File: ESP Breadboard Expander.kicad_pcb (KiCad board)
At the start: 2 copper layers, 88.3 x 51 mm, 20 parts, among them J1 Conn_02x04_Odd_Even, J10 PJ-063BH, J2 Conn_01x08_Socket, J3 Conn_01x08_Socket, J4 Conn_01x19_Socket, J5 Conn_01x19_Socket, J6 Conn_01x14_Pin, J7 Conn_01x14_Pin, J8 Conn_01x02_Pin, J9 Conn_01x02_Pin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

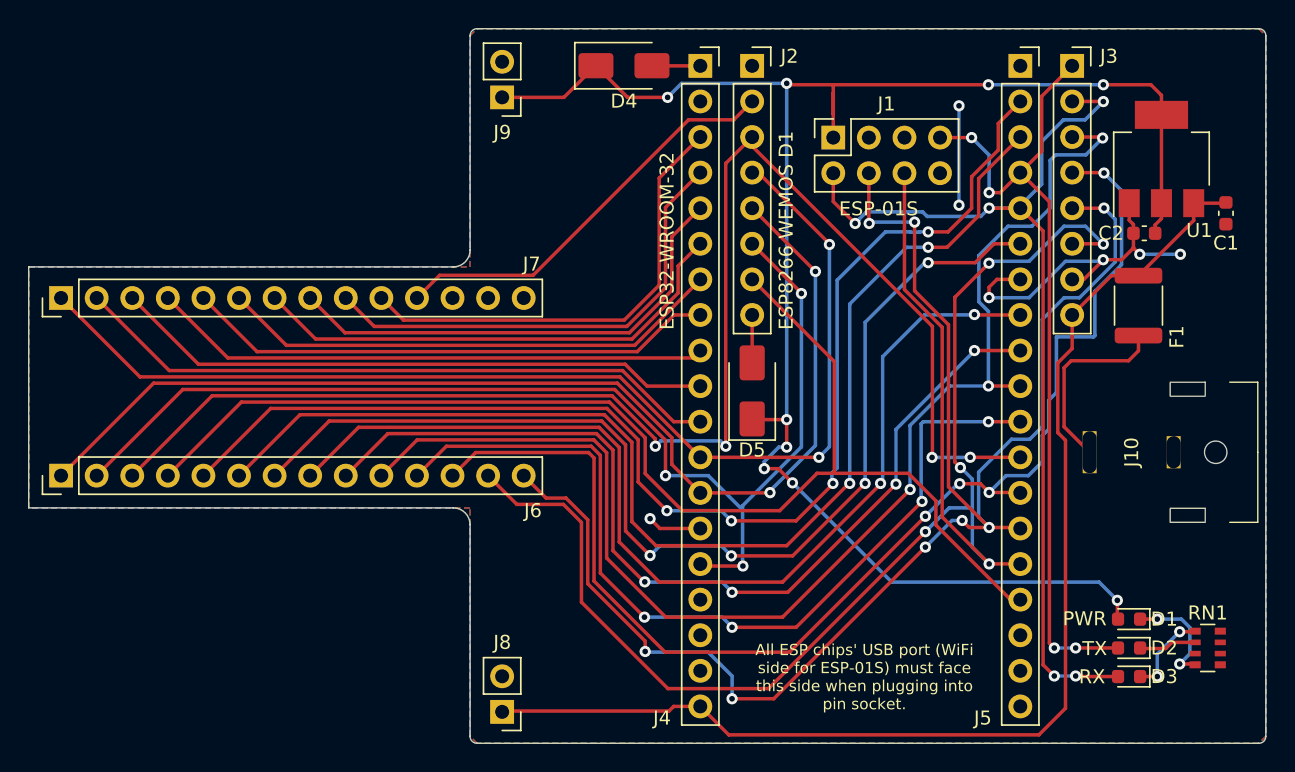
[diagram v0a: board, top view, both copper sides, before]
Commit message: Removed diode for 3.3V power from ESP to breadboard
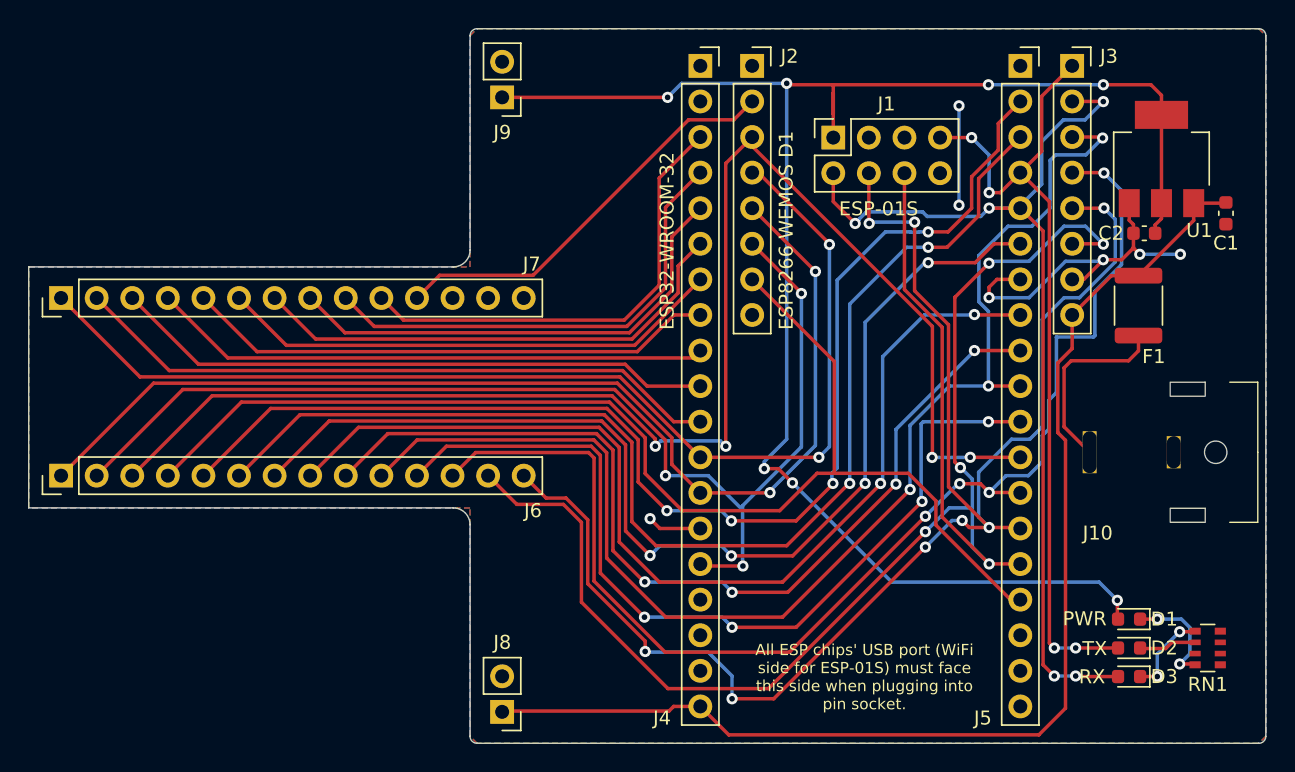
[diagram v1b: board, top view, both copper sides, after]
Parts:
- removed D4, D5: D_Small, Diode_SMD:D_SMA
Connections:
- J2 pad 8: Net-(D5-A) -> unconnected-(J2-Pin_8-Pad8)
- J4 pad 1: Net-(D4-A) -> unconnected-(J4-Pin_1-Pad1)
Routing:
- net +3.3V: track 126.5 -> 121.8 mm, vias 9 -> 7
- net Net-(D4-A): track 3.45 -> 0.00 mm
- net Net-(D5-A): track 3.42 -> 0.00 mm

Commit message: Improved GND traces
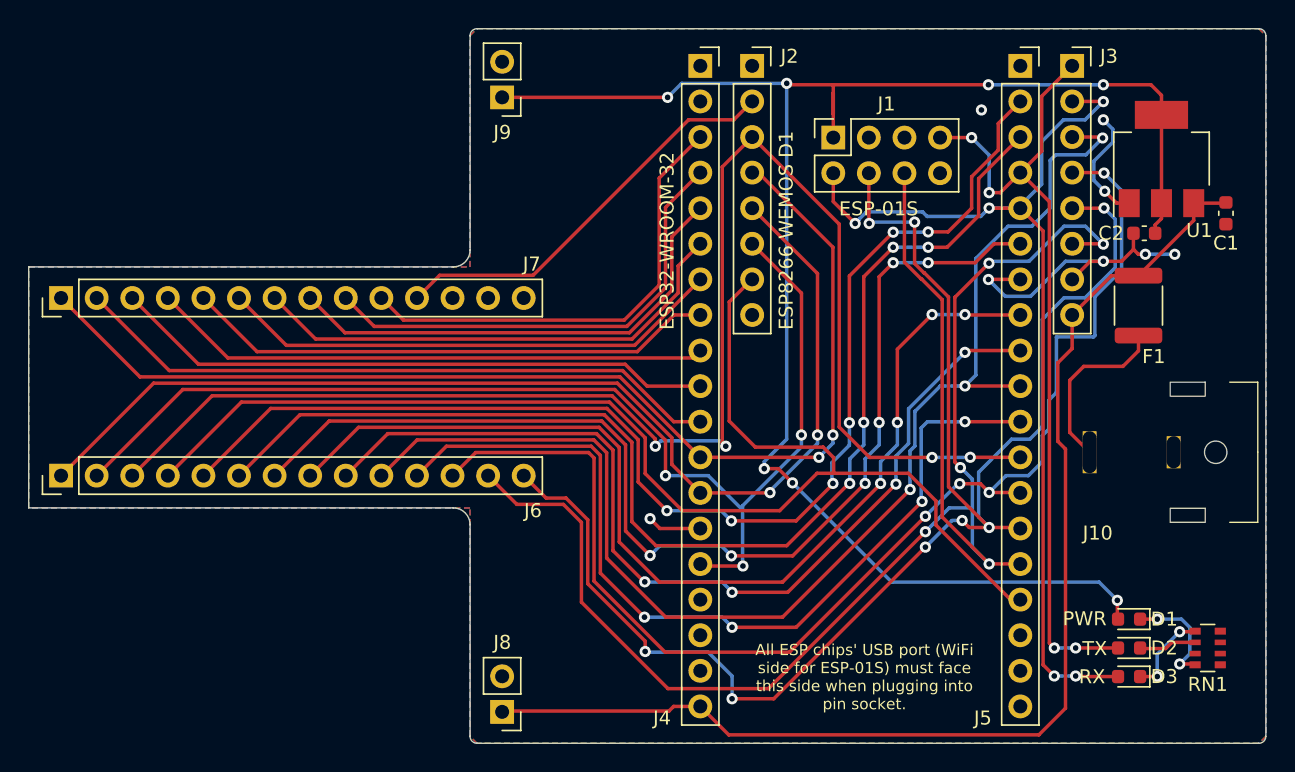
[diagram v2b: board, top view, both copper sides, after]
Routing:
- net /IO15: track 89.9 -> 94.0 mm
- net /IO16: track 104.2 -> 107.0 mm
- net GND: track 35.6 -> 33.8 mm, vias 7 -> 8
- net /IO21: track 79.0 -> 80.3 mm, vias 4 -> 6
- net Net-(F1-Pad1): track 13.8 -> 12.7 mm
- net /IO22: track 85.9 -> 86.4 mm, vias 2 -> 4
- net /IO5: track 91.9 -> 92.5 mm
- net /IO23: track 88.6 -> 88.3 mm, vias 4 -> 6
- net /IO19: track 73.8 -> 73.5 mm, vias 2 -> 4

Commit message: Added more labeling & checked some JLCPCB capabilities
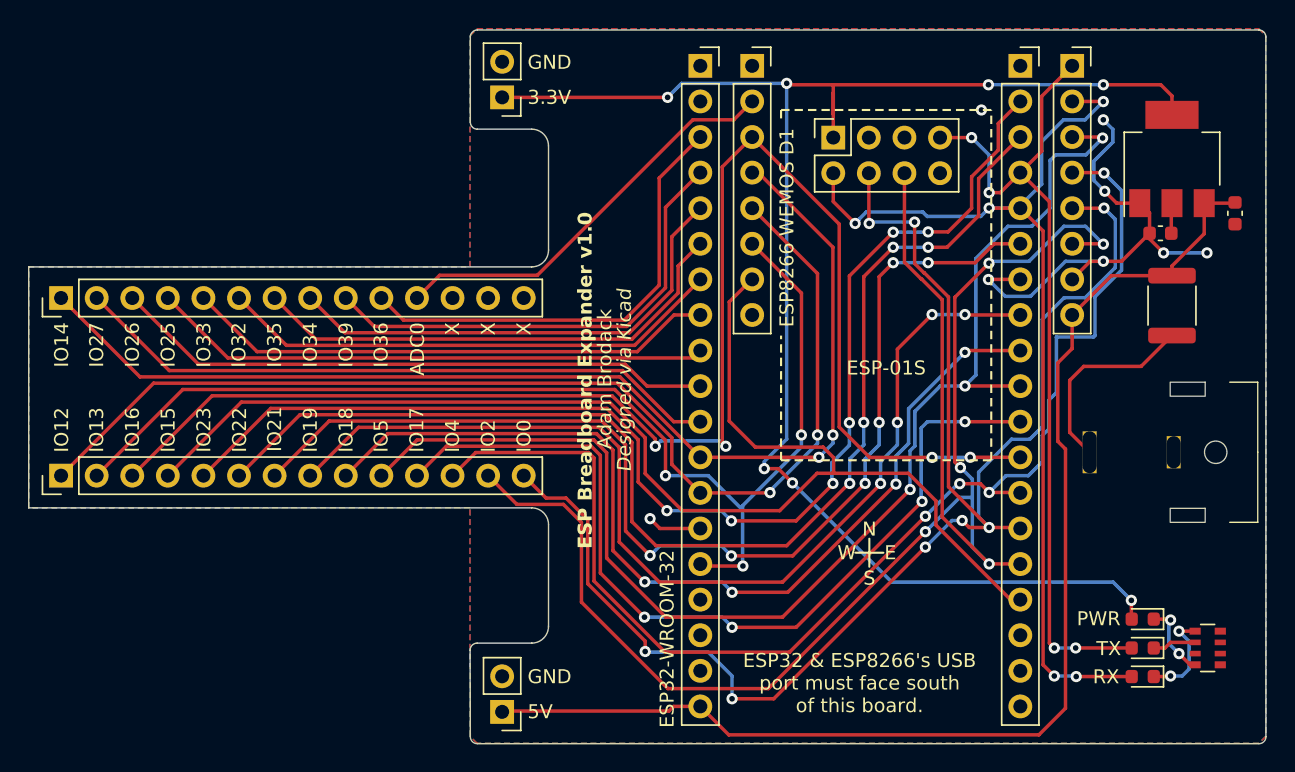
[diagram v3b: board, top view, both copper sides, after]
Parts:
- moved F1 2.39 mm to (121.6, 62.8)
- moved C2 1.15 mm to (120.8, 57.6)
- moved D1 0.98 mm to (119.5, 85.1)
- moved D2 0.98 mm to (119.5, 87.2)
- moved D3 0.98 mm to (119.5, 89.2)
- moved U1 0.75 mm to (121.6, 52.3)
- moved C1 0.65 mm to (126.1, 56.2)
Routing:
- net GND: track 33.8 -> 39.2 mm
- net +3.3V: track 121.8 -> 117.0 mm
- net Net-(D1-K): track 7.82 -> 5.54 mm
- net Net-(F1-Pad1): track 12.7 -> 14.4 mm
- net +5V: track 85.8 -> 87.4 mm
- net Net-(D2-K): track 4.12 -> 3.12 mm
- net /TX: track 58.2 -> 59.1 mm
- net /RX: track 71.0 -> 72.0 mm
- net Net-(D3-K): track 6.20 -> 6.96 mm
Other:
- board size 88.3 x 51 mm -> 88.3 x 50.9 mm
- board text added: "3.3V"
- board text added: "5V"
- board text added: "ADC0"
- board text added: "Adam Brodack"
- board text added: "Designed via Kicad"
- board text added: "E"
- board text added: "ESP Breadboard Expander v1.0"
- board text added: "ESP32 & ESP8266's USB port must face south of this board."
- board text added: "GND"
- board text added: "IO0"
- board text added: "IO12"
- board text added: "IO13"
- board text added: "IO14"
- board text added: "IO15"
- board text added: "IO16"
- board text added: "IO17"
- board text added: "IO18"
- board text added: "IO19"
- board text added: "IO2"
- board text added: "IO21"
- board text added: "IO22"
- board text added: "IO23"
- board text added: "IO25"
- board text added: "IO26"
- board text added: "IO27"
- board text added: "IO32"
- board text added: "IO33"
- board text added: "IO34"
- board text added: "IO35"
- board text added: "IO36"
- board text added: "IO39"
- board text added: "IO4"
- board text added: "IO5"
- board text added: "N"
- board text added: "S"
- board text added: "W"
- board text added: "X"
- board text removed: "All ESP chips' USB port (WiFi side for ESP-01S) must face this side when plugging into pin socket."

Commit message: Fixed all errors found by DRC
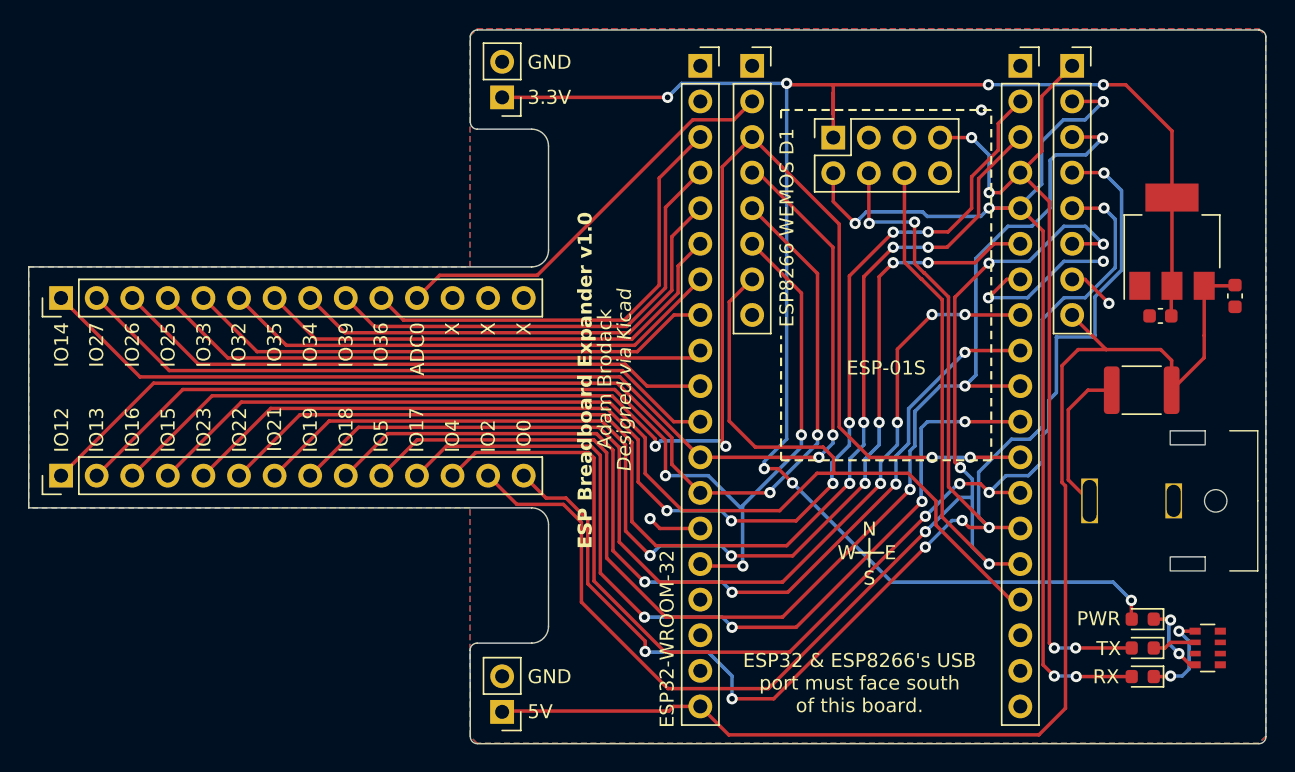
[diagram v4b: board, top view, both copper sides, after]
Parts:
- moved F1 6.41 mm to (119.4, 68.8), turned to 0 degrees
- moved C1 5.90 mm to (126.1, 62.1)
- moved U1 5.90 mm to (121.6, 58.2)
- moved C2 5.90 mm to (120.8, 63.5)
- moved J10 3.47 mm to (110.7, 76.7)
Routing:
- net GND: track 39.2 -> 19.3 mm, vias 8 -> 5
- net +3.3V: track 117.0 -> 127.7 mm
- net +5V: track 87.4 -> 91.4 mm
- net Net-(F1-Pad1): track 14.4 -> 10.8 mm

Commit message: Fixed a number of issues to work with JLCPCB
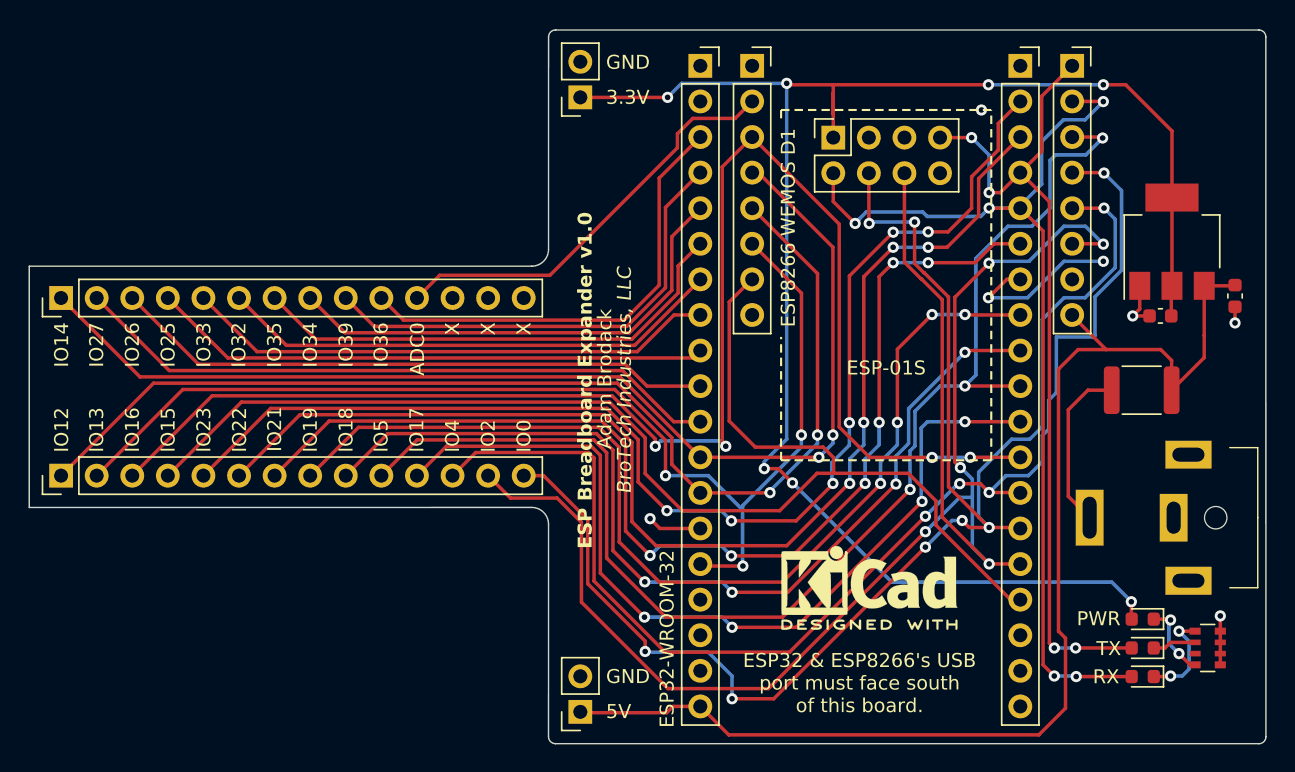
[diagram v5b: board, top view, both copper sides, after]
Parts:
- added REF**: KiCad-Logo2_5mm_SilkScreen, Symbol:KiCad-Logo2_5mm_SilkScreen, F.Cu at (100.0, 82.9)
- D3: value Blue -> Yellow
- J8, J9: value Conn_01x02_Pin -> Conn_01x02_Socket; footprint Adam_Custom_Footprints:PinHeader_1x02_P2.54mm_Vertical_UpSideDown -> Connector_PinSocket_2.54mm:PinSocket_1x02_P2.54mm_Vertical
- moved J8 5.58 mm to (79.4, 91.8)
- moved J9 5.58 mm to (79.4, 47.9)
- moved J10 1.20 mm to (110.7, 77.9)
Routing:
- net +3.3V: track 127.7 -> 122.1 mm
- net +5V: track 91.4 -> 86.1 mm
- net GND: track 19.3 -> 24.2 mm, vias 5 -> 7
- net Net-(F1-Pad1): track 10.8 -> 12.0 mm
- net /ADC0: track 29.7 -> 30.3 mm
- added copper zone on In1.Cu, net GND
- added copper zone on In2.Cu, net GND
- removed copper zone on B.Cu, net GND
- removed copper zone on F.Cu, net GND
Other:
- outline, holes or cut-outs redrawn
- copper layers 2 -> 4
- board text added: "${COMPANY}"
- board text added: "ESP Breadboard Expander ${REVISION}"
- board text removed: "Designed via Kicad"
- board text removed: "E"
- board text removed: "ESP Breadboard Expander v1.0"
- board text removed: "N"
- board text removed: "S"
- board text removed: "W"

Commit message: Fixed LED circuit & position of them
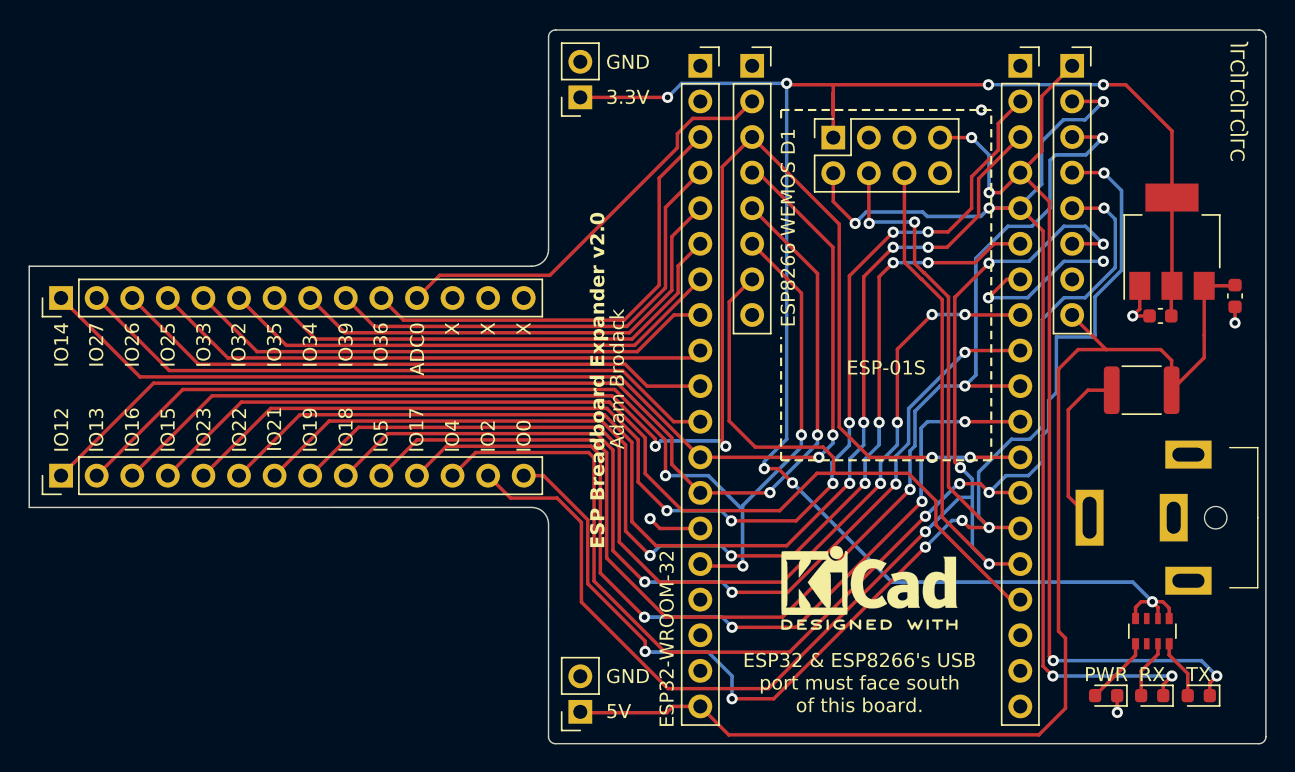
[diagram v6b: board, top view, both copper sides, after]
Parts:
- moved D1 6.05 mm to (116.9, 90.6)
- moved D3 4.22 mm to (123.5, 90.6)
- moved RN1 4.13 mm to (120.2, 86.0), turned to 90 degrees
- moved D2 3.47 mm to (120.2, 90.6)
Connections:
- D1 pad 1: Net-(D1-K) -> GND
- D1 pad 2: +3.3V -> Net-(D1-A)
- D2 pad 1: Net-(D2-K) -> /RX
- D2 pad 2: /TX -> Net-(D2-A)
- D3 pad 1: Net-(D3-K) -> /TX
- D3 pad 2: /RX -> Net-(D3-A)
- RN1 pad 1: GND -> Net-(D1-A)
- RN1 pad 2: GND -> unconnected-(RN1-R2.1-Pad2)
- RN1 pad 3: GND -> Net-(D2-A)
- RN1 pad 4: GND -> Net-(D3-A)
- RN1 pad 5: Net-(D3-K) -> +3.3V
- RN1 pad 6: Net-(D2-K) -> +3.3V
- RN1 pad 8: Net-(D1-K) -> +3.3V
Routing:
- net /TX: track 59.1 -> 68.2 mm
- net Net-(D3-K): track 6.96 -> 0.00 mm, vias 2 -> 0
- net +3.3V: track 122.1 -> 128.0 mm
- net Net-(D1-K): track 5.54 -> 0.00 mm, vias 2 -> 0
- net Net-(D1-A): track 0.00 -> 4.90 mm
- net /RX: track 72.0 -> 76.6 mm
- net Net-(D3-A): track 0.00 -> 4.25 mm
- net Net-(D2-A): track 0.00 -> 4.20 mm
- net Net-(D2-K): track 3.12 -> 0.00 mm
- net GND: track 24.2 -> 21.9 mm
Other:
- board text added: "JLCJLCJLCJLC"
- board text removed: "${COMPANY}"
